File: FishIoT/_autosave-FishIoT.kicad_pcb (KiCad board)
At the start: 4 copper layers, 42 x 70 mm, 117 parts, among them IC1 RV-3032-C7_32.768KHZ-2.5PPM-T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, J1 USB4105-GF-A-120, J3 Conn_Coaxial, J4 BM05B-ZESS-TBT, J5 SF72S006VBDR2500, J6 Conn_Coaxial, J7 SHF-105-01-L-D-SM, J8 0705430001, SW1 PTS645SM43SMTR92 LF, SW2 PTS645SM43SMTR92 LF, SW3 PTS645SM43SMTR92 LF, U1 USBLC6-2P6, U2 NRF9151-LACA-R7, U3 CP2102N-Axx-xQFN20, U4 MAX-M10S, U5 TPD3F303DPVR, U6 MAX3471, U7 SI1040X-T1-GE3, U8 TPS63000

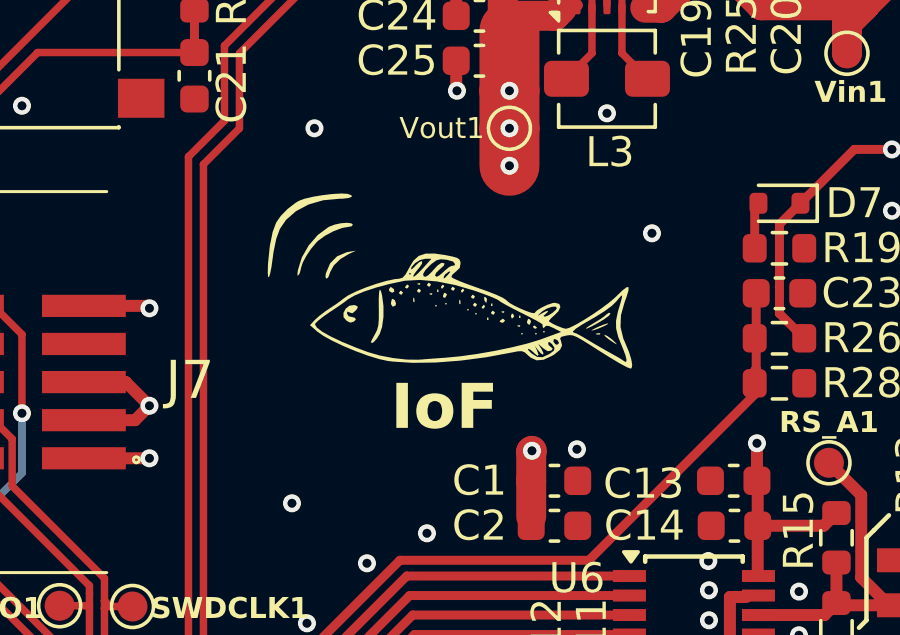
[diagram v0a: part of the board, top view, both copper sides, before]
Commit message: v26.0
First draft of schematics and PCB with nRF9151
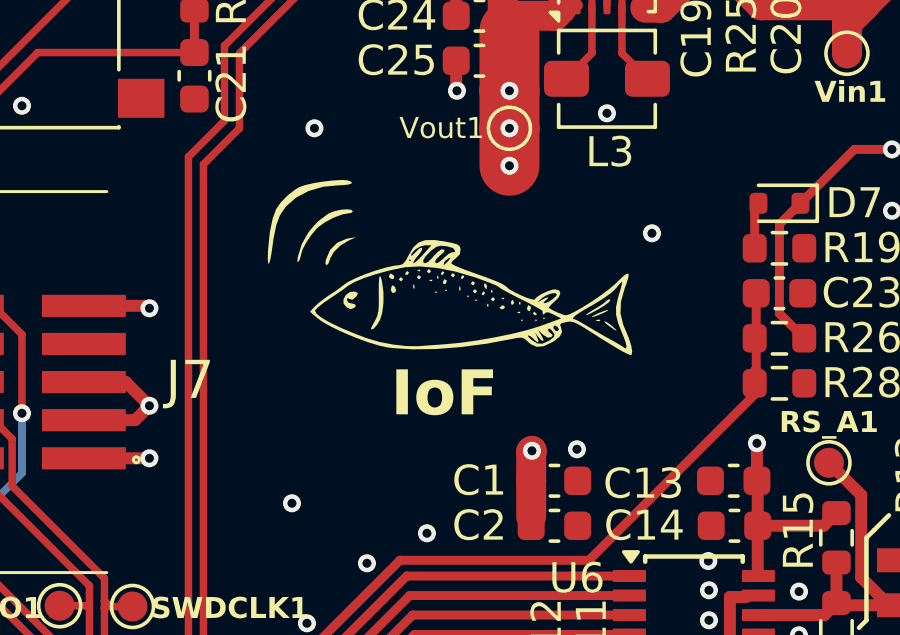
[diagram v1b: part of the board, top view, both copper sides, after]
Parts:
- moved G*** 0.45 mm to (112.0, 56.8)
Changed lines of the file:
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@@
 	(footprint "FishIoT_Footprint_library:Fishlogo"
 		(layer "F.Cu")
-		(at 112 57.25)
+		(at 112 56.8)
 		(property "Reference" "G***"
 			(at 0 0 0)
@@
 	)
 	(gr_text "IoF"
-		(at 109.789607 61.6696 0)
+		(at 109.789607 61.2196 0)
 		(layer "F.SilkS")
 		(effects
